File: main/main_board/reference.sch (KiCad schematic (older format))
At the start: 20 parts, among them U1 MAX6220ASA-5.0+, U2 OPA209

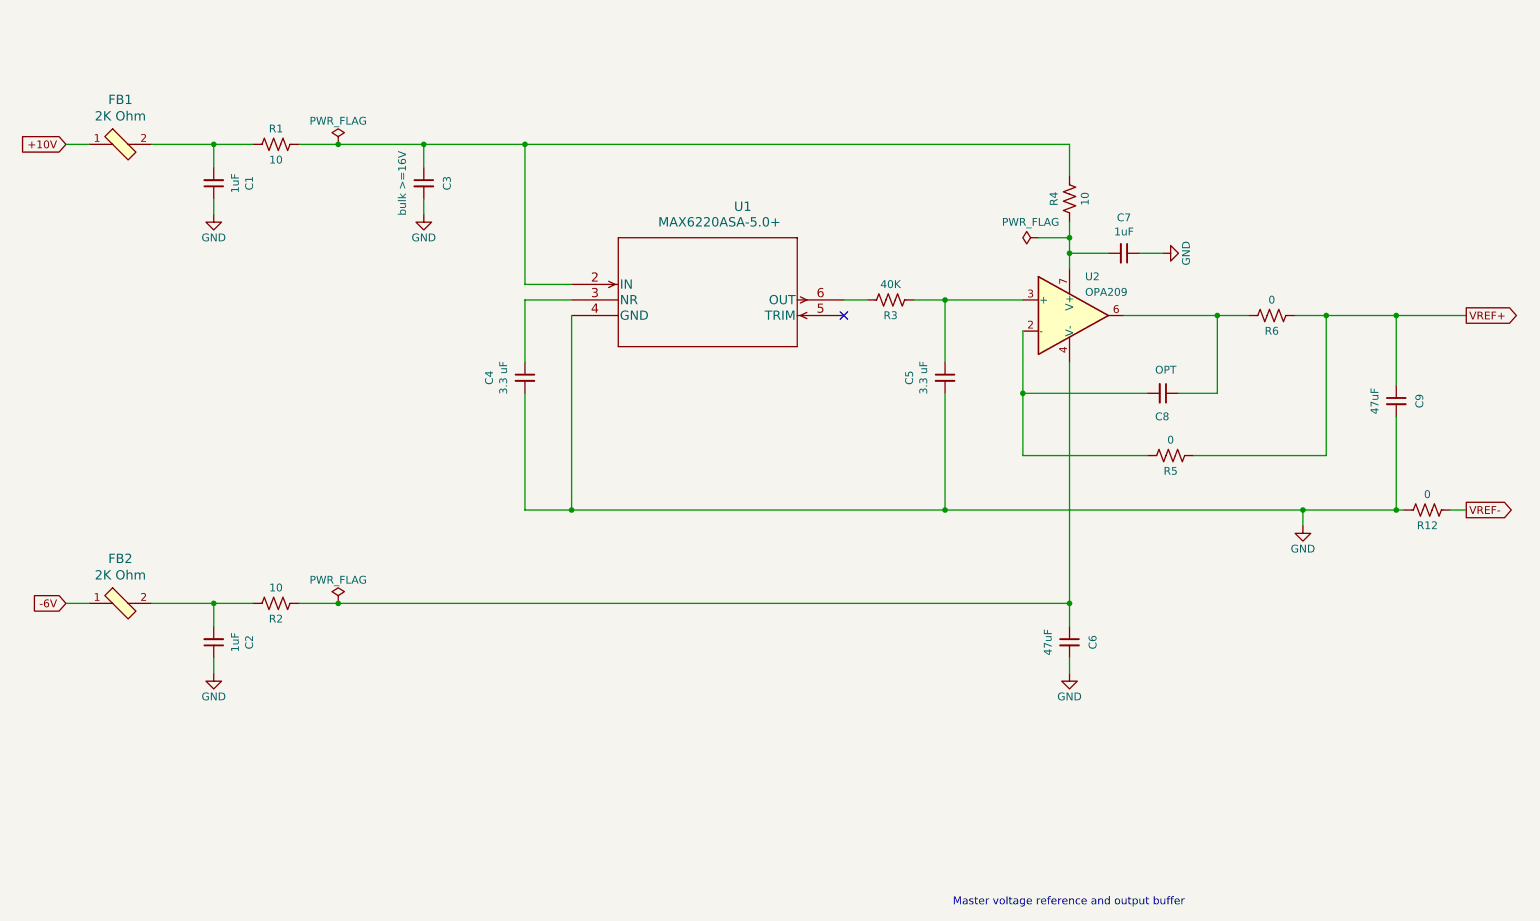
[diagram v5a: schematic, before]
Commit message: Various preparations for routing the main board. Cleaned up the BOM and reconciled it with the Digikey BOM, so lots of component attributes have changed. This involved pinning down some components which had been vague, especially ferrite beads and chip capacitors. 1uF capacitors have all been changed to 10uF. Changed CARDSEL lines to be buffered rather than filtered, since we had the unused buffers sitting there. Another pass on the Microzed pin mapping.  Brought out the DEBUG LVDS line, and tweaked orderings. Added RC filter and pullups on I2C and PROBE_CONFIG.  We might need level translators here to get >=3.3V Added mount holes for the low volt regulator daughtercard, and dimensioned the connector location.
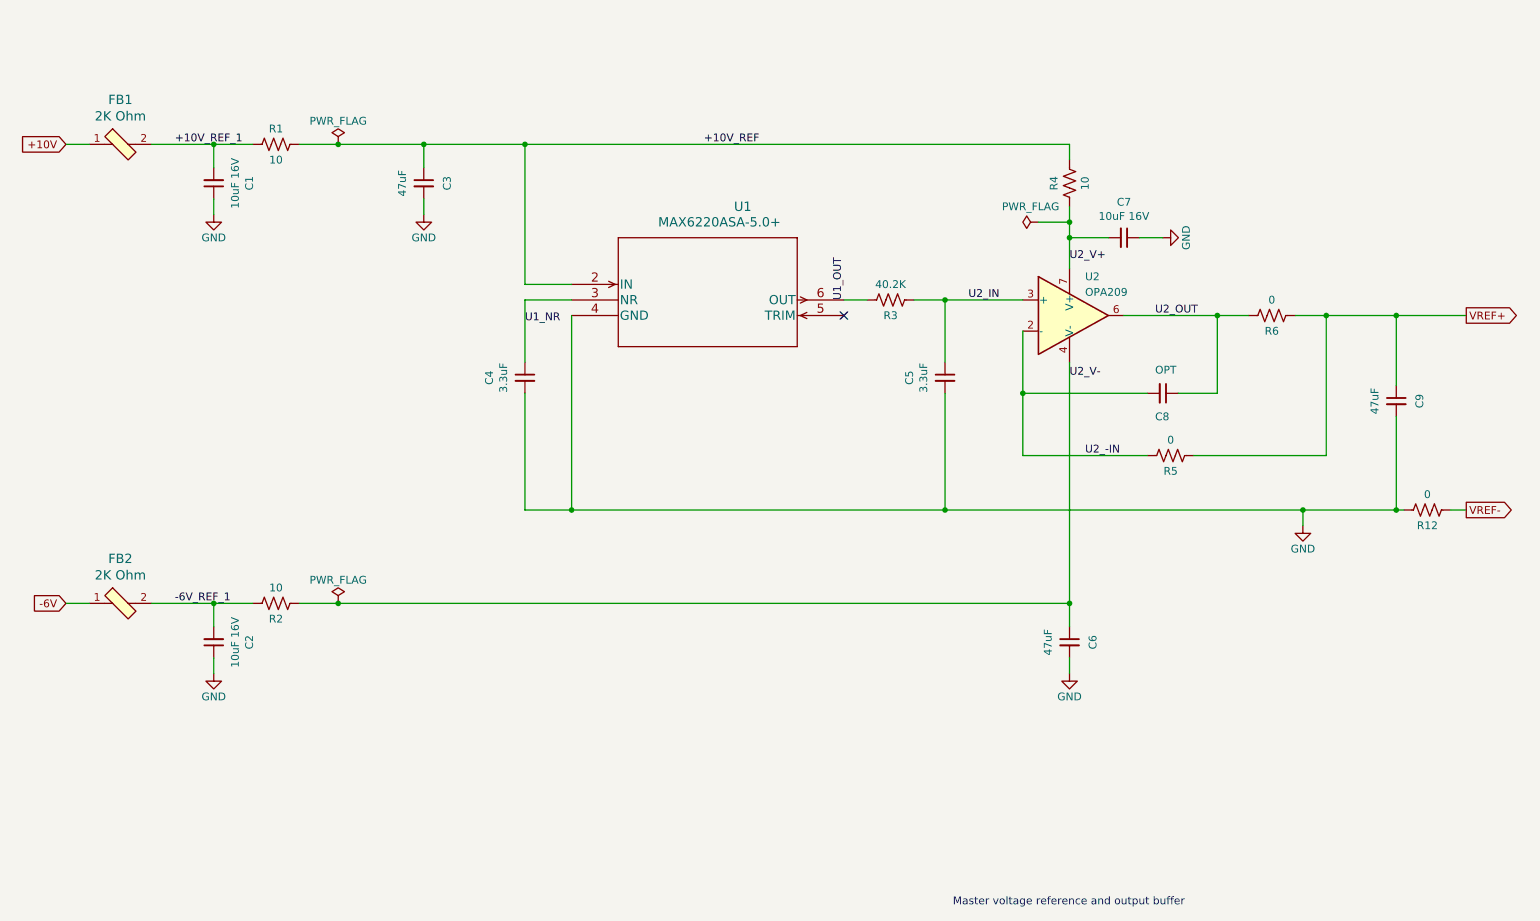
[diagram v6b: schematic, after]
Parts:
- C1, C2, C7: value 1uF -> 10uF 16V; DK line 27 -> 10; Description CAP CER 1UF 16V X7R 0805 -> CAP CER 10UF 16V X5R 0805; Digikey 1276-6471-1-ND -> 399-8012-1-ND; MPN CL21B105KOFNNNG -> C0805C106K4PACTU; Manufacturer Samsung Electro-Mechanics -> KEMET
- C3: value bulk >=16V -> 47uF; DK line (none) -> 11; Description (none) -> CAP CER 47UF 16V X5R 1210; Digikey (none) -> 399-5514-1-ND; MPN (none) -> C1210C476M4PACTU; Manufacturer (none) -> KEMET
- C4, C5: value 3.3 uF -> 3.3uF; DK line (none) -> 6; Description (none) -> CAP FILM 3.3UF 5% 63VDC RADIAL
- C6, C9: DK line 28 -> 11; Description CAP CER 47UF 6.3V X7R 1210 -> CAP CER 47UF 16V X5R 1210; Digikey 399-5516-1-ND -> 399-5514-1-ND; MPN C1210C476M9RACTU -> C1210C476M4PACTU
- C8: MPN (none) -> DNP; Manufacturer (none) -> DNP
- FB1, FB2: Category Filters -> (none); DK line 5 -> 16; DK_Datasheet_Link https://product.tdk.com/info/en/catalog/datasheets/beads_co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 -> (none); DK_Detail_Page /product-detail/en/tdk-corporation/MPZ2012S601AT000/445-220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 -> (none); Digi-Key_PN 240-2396-1-ND -> (none); Status Active -> (none)
- R1, R2, R4: DK line (none) -> 30; Description (none) -> RES 10 OHM 1% 1/8W 0603; Digikey (none) -> RNCP0603FTD10R0CT-ND; MPN (none) -> RNCP0603FTD10R0; Manufacturer (none) -> Stackpole Electronics Inc
- R12, R5, R6: DK line (none) -> 12; Description (none) -> RES 0 OHM JUMPER 1/10W 0603; Digikey (none) -> RMCF0603ZT0R00CT-ND; MPN (none) -> RMCF0603ZT0R00; Manufacturer (none) -> Stackpole Electronics Inc
- R3: value 40K -> 40.2K; DK line (none) -> 14; Description (none) -> RES 40.2K OHM 1% 1/8W 0603; Digikey (none) -> RNCP0603FTD40K2CT-ND; MPN (none) -> RNCP0603FTD40K2; Manufacturer (none) -> Stackpole Electronics Inc
- U1: DK line (none) -> 4; Description (none) -> IC VREF SERIES 0.1% 8SOIC
- U2: DK line (none) -> 5
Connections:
- net -6V_REF_1: now reaches C2.2, FB2.2, R2.2
- net +10V_REF_1: now reaches C1.2, FB1.2, R1.1
- net +10V_REF: now reaches C3.1, R1.2, R4.2, U1.2 (IN)
- net U1_NR: now reaches C4.1, U1.3 (NR)
- net U1_OUT: now reaches R3.2, U1.6 (OUT)
- net U2_IN: now reaches C5.1, R3.1, U2.3 (+)
- net U2_OUT: now reaches C8.1, R6.2, U2.6
- net U2_-IN: now reaches C8.2, R5.2, U2.2 (-)
- net U2_V+: now reaches C7.2, R4.1, U2.7 (V+)
- net U2_V-: now reaches C6.1, R2.1, U2.4 (V-)
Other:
- moved on the sheet: C7, R4

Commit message: Main board is now fully routed and passing DRC. Minor changes related to pin remapping. I2C and one-wire pullups are to OVDD 3.3V, not VCCIO 2.5V. Changes to supply decoupling and VREF- net in reference.sch, suggested by routing.
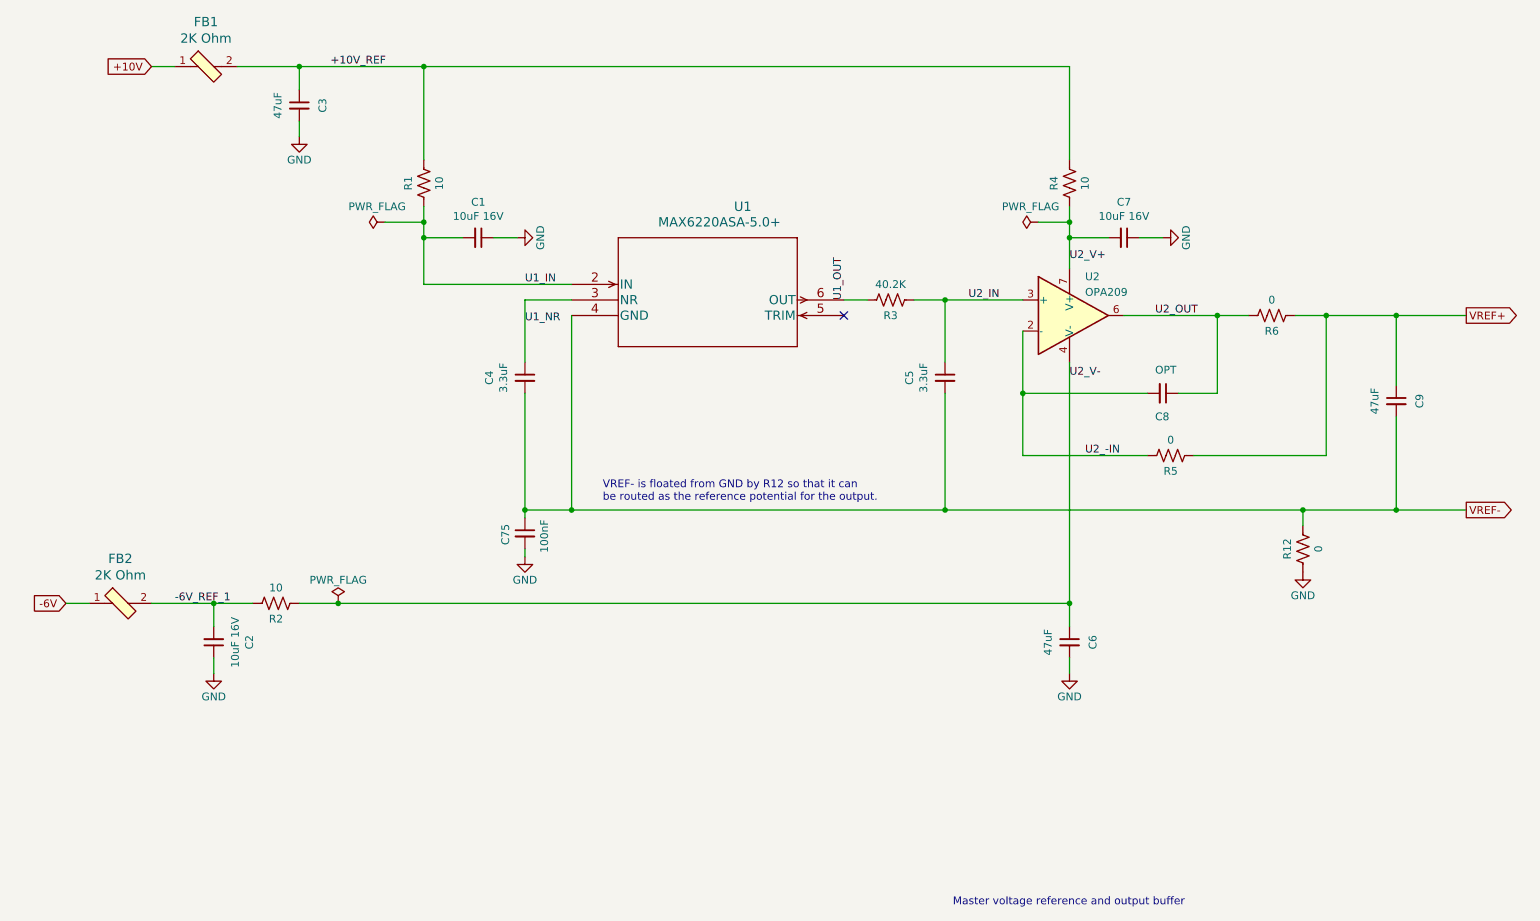
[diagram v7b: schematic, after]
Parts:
- added C75: 100nF, Capacitor_SMD:C_0603_1608Metric, symbol Device:C_Small
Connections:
- net +10V_REF: now also FB1.2, R1.1; no longer R1.2, U1.2 (IN)
- net GND: now also R12.1, C75.2; no longer C4.2, C5.2, C9.2, R12.2, U1.4 (GND)
- net VREF-: now also C4.2, C5.2, C9.2, R12.2, U1.4 (GND), C75.1; no longer R12.1
- removed net +10V_REF_1: C1.2, FB1.2, R1.1
- new net U1_IN: C1.2, R1.2, U1.2 (IN)
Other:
- note added: "VREF- is floated from GND by R12 so that it can \nbe routed as the reference potential for the output."
- moved on the sheet: C1, C3, FB1, R1, R12

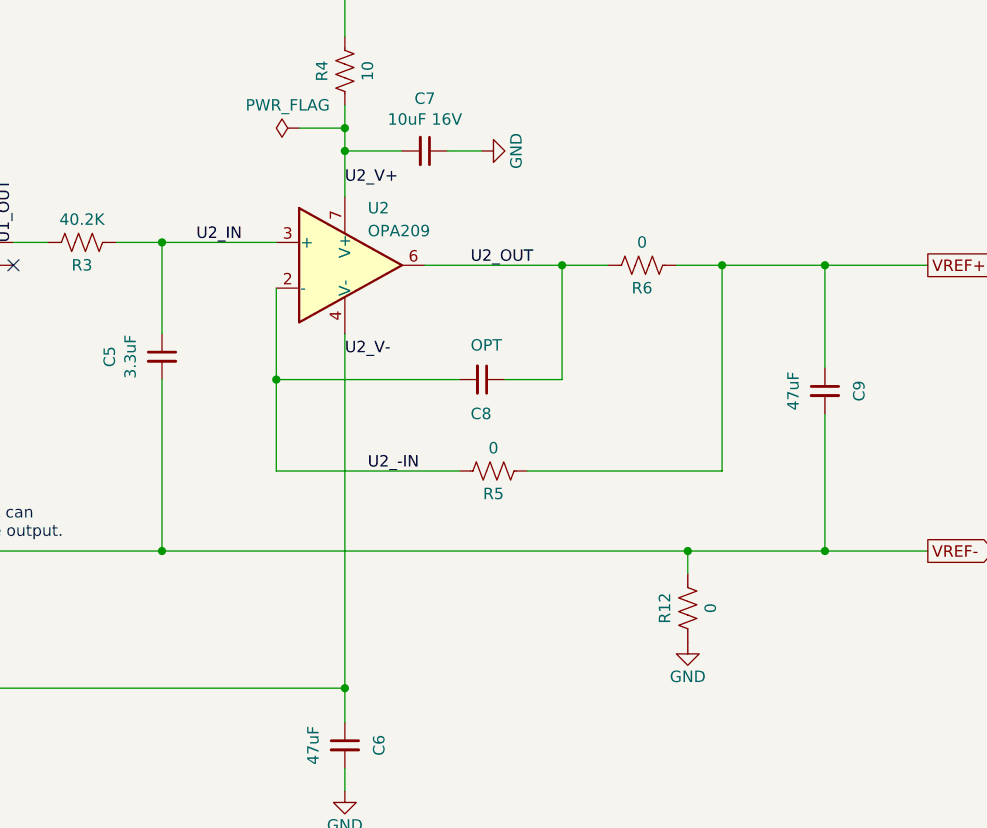
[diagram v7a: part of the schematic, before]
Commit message: Added testpoints, debug IO port, LEDs, and clock output jack.
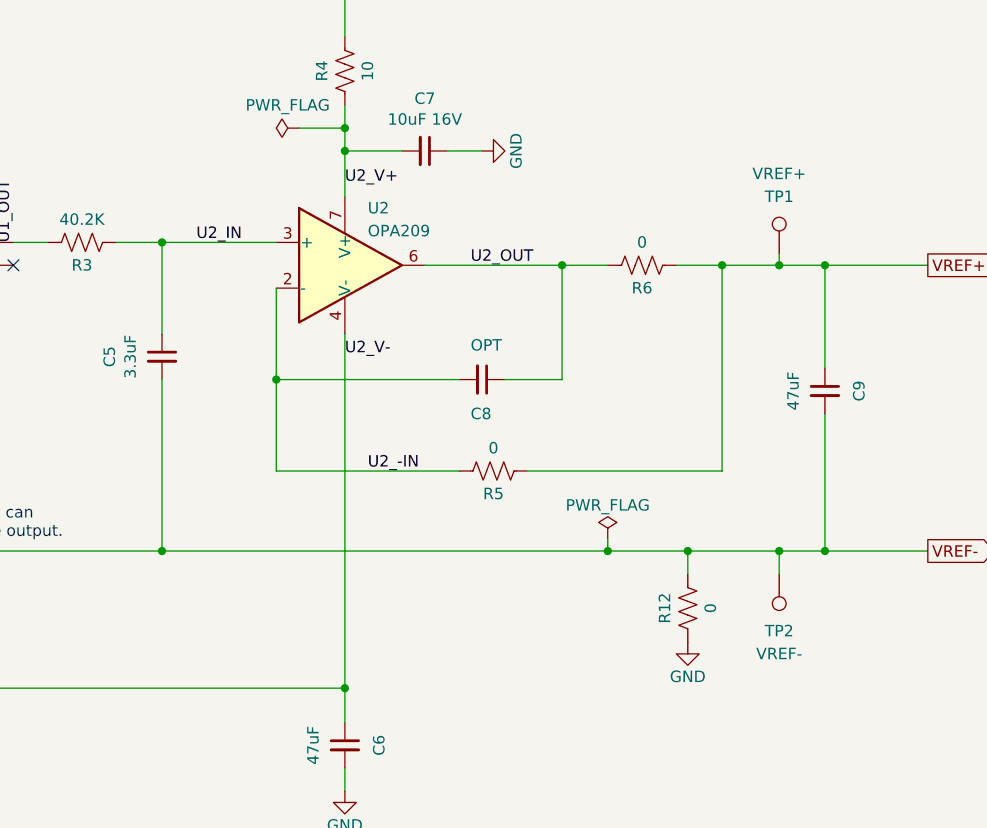
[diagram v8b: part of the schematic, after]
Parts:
- added TP1: VREF+, TestPoint:TestPoint_Keystone_5000-5004_Miniature, symbol Connector:TestPoint
- added TP2: VREF-, TestPoint:TestPoint_Keystone_5000-5004_Miniature, symbol Connector:TestPoint
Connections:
- net VREF+: now also TP1.1
- net VREF-: now also TP2.1
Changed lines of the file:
@@
 Connection ~ 9500 2950
 Wire Wire Line
-	9500 2950 9950 2950
+	9500 2950 9750 2950
 Wire Wire Line
 	8200 2950 8800 2950
 Connection ~ 8800 2950
 Wire Wire Line
-	7050 4200 9350 4200
+	7050 4200 9000 4200
 Wire Wire Line
 	4650 4200 7050 4200
@@
 	2350 4800 2600 4800
 Connection ~ 2350 4800
-Wire Wire Line
-	3150 4800 7850 4800
 Connection ~ 3150 4800
 Connection ~ 7850 4800
@@
 U1_IN
 Wire Wire Line
-	9350 4200 9950 4200
+	9350 4200 9750 4200
 Connection ~ 9350 4200
 Connection ~ 9950 4200
@@
 Text Notes 4850 4150 0    50   ~ 0
 VREF- is floated from GND by R12 so that it can \nbe routed as the reference potential for the output.
+$Comp
+L Connector:TestPoint TP?
+U 1 1 5F15CA95
+P 9750 2900
+AR Path="/5DFCF14D/5DA78AA2/5F15CA95" Ref="TP?"  Part="1"
+AR Path="/5DFCF14D/5E295469/5F15CA95" Ref="TP?"  Part="1"
+AR Path="/5DFCF14D/5E195558/5F15CA95" Ref="TP?"  Part="1"
+AR Path="/5F15CA95" Ref="TP?"  Part="1"
+AR Path="/5E525FC9/5F15CA95" Ref="TP?"  Part="1"
+AR Path="/5E525EB8/5F15CA95" Ref="TP1"  Part="1"
+F 0 "TP1" H 9750 3150 50  0000 C CNN
+F 1 "VREF+" H 9750 3250 50  0000 C CNN
+F 2 "TestPoint:TestPoint_Keystone_5000-5004_Miniature" H 9950 2900 50  0001 C CNN
+F 3 "~" H 9950 2900 50  0001 C CNN
+F 4 "Do Not Populate" H 9750 2900 50  0001 C CNN "Description"
+F 5 "DNP" H 9750 2900 50  0001 C CNN "MPN"
+	1    9750 2900
+	1    0    0    -1
+$EndComp
+$Comp
+L Connector:TestPoint TP?
+U 1 1 5F15E224
+P 9750 4300
+AR Path="/5DFCF14D/5DA78AA2/5F15E224" Ref="TP?"  Part="1"
+AR Path="/5DFCF14D/5E295469/5F15E224" Ref="TP?"  Part="1"
+AR Path="/5DFCF14D/5E195558/5F15E224" Ref="TP?"  Part="1"
+AR Path="/5F15E224" Ref="TP?"  Part="1"
+AR Path="/5E525FC9/5F15E224" Ref="TP?"  Part="1"
+AR Path="/5E525EB8/5F15E224" Ref="TP2"  Part="1"
+F 0 "TP2" H 9750 4550 50  0000 C CNN
+F 1 "VREF-" H 9750 4650 50  0000 C CNN
+F 2 "TestPoint:TestPoint_Keystone_5000-5004_Miniature" H 9950 4300 50  0001 C CNN
+F 3 "~" H 9950 4300 50  0001 C CNN
+F 4 "Do Not Populate" H 9750 4300 50  0001 C CNN "Description"
+F 5 "DNP" H 9750 4300 50  0001 C CNN "MPN"
+	1    9750 4300
+	-1   0    0    1
+$EndComp
+Wire Wire Line
+	9750 4300 9750 4200
+Wire Wire Line
+	9750 2900 9750 2950
+Connection ~ 9750 2950
+Wire Wire Line
+	9750 2950 9950 2950
+Connection ~ 9750 4200
+Wire Wire Line
+	9750 4200 9950 4200
+$Comp
+L power:PWR_FLAG #FLG?
+U 1 1 5F2F69F5
+P 9000 4150
+AR Path="/5E62FD57/5E630FEC/5F2F69F5" Ref="#FLG?"  Part="1"
+AR Path="/5E525EB8/5F2F69F5" Ref="#FLG0107"  Part="1"
+F 0 "#FLG0107" H 9000 4225 50  0001 C CNN
+F 1 "PWR_FLAG" H 9000 4300 50  0000 C CNN
+F 2 "" H 9000 4150 50  0001 C CNN
+F 3 "~" H 9000 4150 50  0001 C CNN
+	1    9000 4150
+	1    0    0    -1
+$EndComp
+Wire Wire Line
+	9000 4150 9000 4200
+Connection ~ 9000 4200
+Wire Wire Line
+	9000 4200 9350 4200
+Wire Wire Line
+	3150 4800 7850 4800
 $EndSCHEMATC
